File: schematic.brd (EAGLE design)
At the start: 100 x 70 mm, 66 parts, among them U1 ADP3338AKCZ-3.3RL7

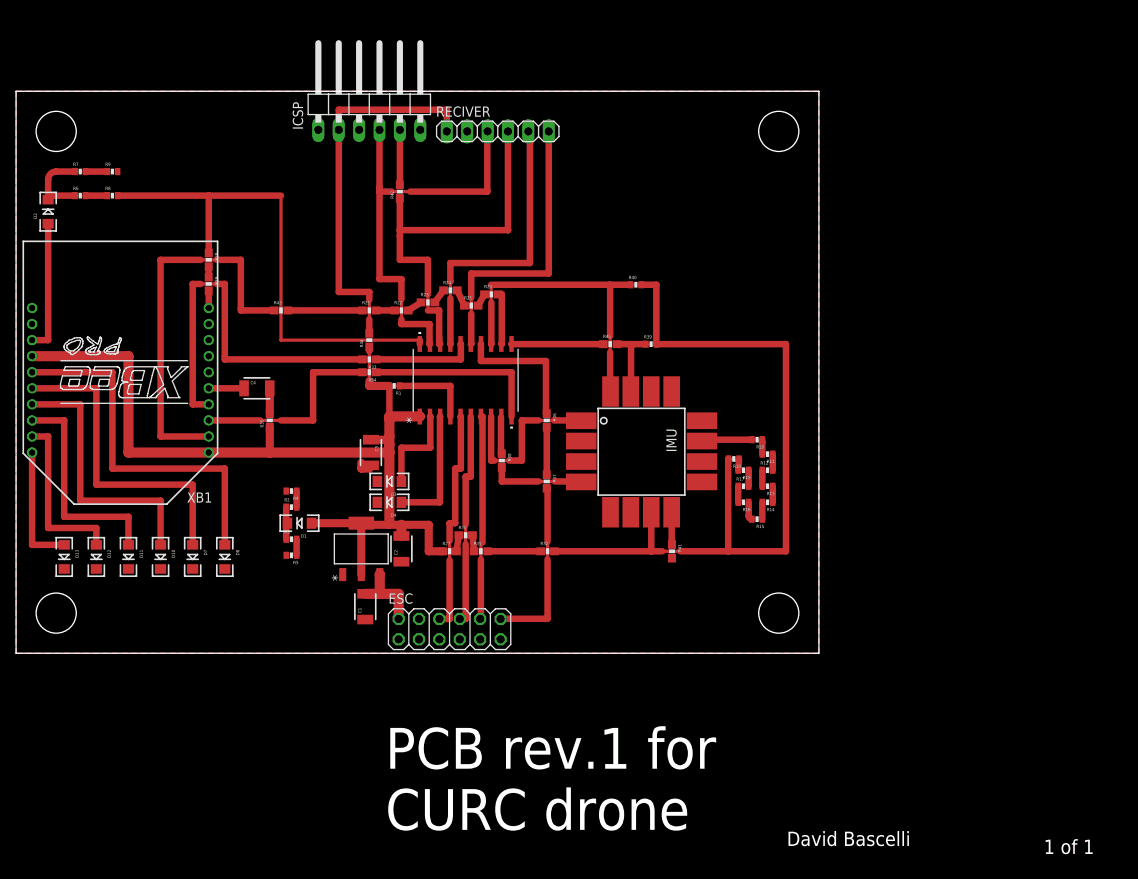
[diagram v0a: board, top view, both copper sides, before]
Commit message: Removed jumper's from schematic and prepared for two layer board
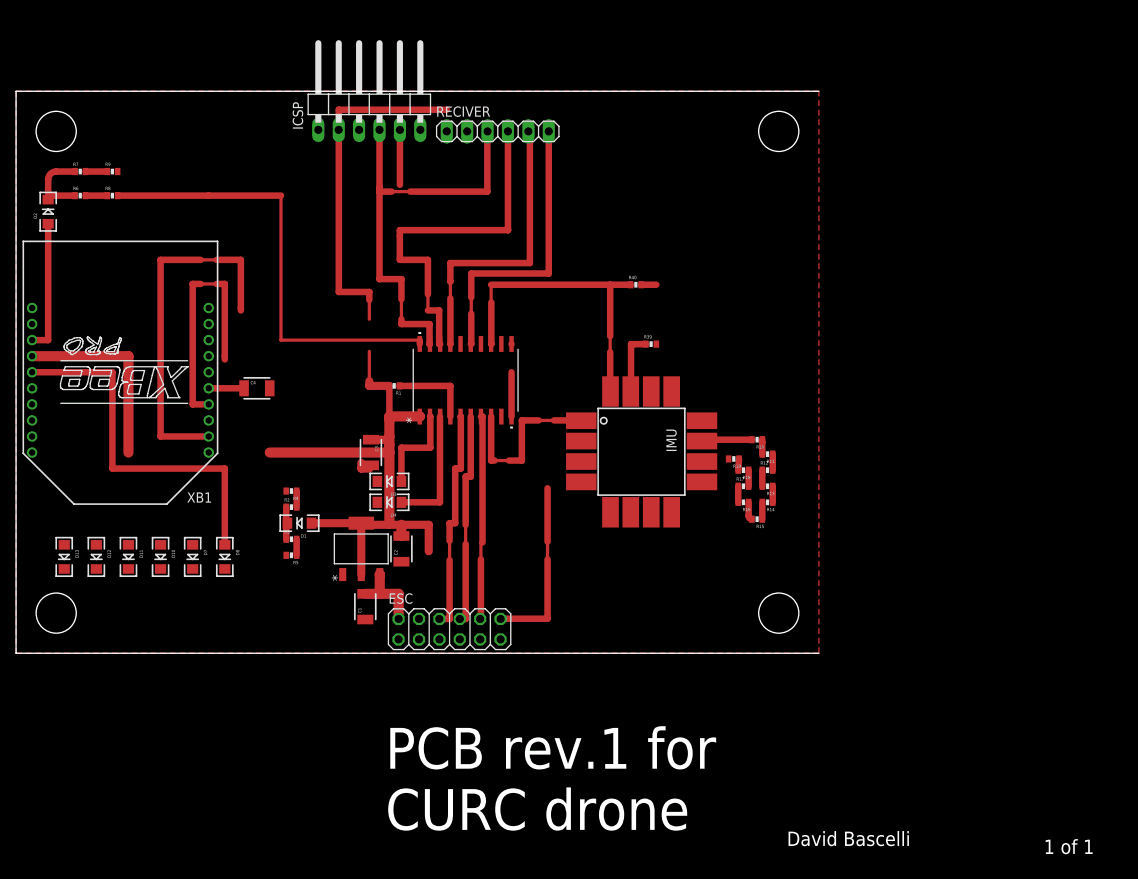
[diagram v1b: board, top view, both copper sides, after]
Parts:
- removed R20, R21, R22, R23, R24, R25, R27, R28, R29, R30, R31, R32, R33, R34, R35, R36, R37, R38, R41, R42, R43, R44, R45: 0, SparkFun-Passives:0603-RES
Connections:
- removed net GND_S: R29.2, XB1.10
- removed net N$1 (its old number): R20.1, R25.2
- removed net N$20 (its old number): R21.2, R22.1
- removed net N$21 (its old number): R22.2, R23.1
- removed net N$22 (its old number): R23.2, R24.1
- removed net N$23 (its old number): R24.2, R25.1
- removed net N$24: R28.2, R29.1
- removed net N$25: MAIN_CONTROLLER.16, R33.1
- removed net N$27: R27.2, R30.1
- removed net N$28: R30.2, R31.1
- removed net N$29: R31.2, R32.1
- removed net N$30: R34.2, XB1.3
- removed net N$31: C4.2, R35.2
- removed net N$32: MAIN_CONTROLLER.14, R36.1
- removed net N$33: R36.2, R37.1
- removed net N$34: IMU.P$4, R38.2
- removed net N$35: IMU.P$8, R41.1
- removed net N$36: R21.1, R43.2
- removed net N$37: ICSP.5, R42.2
- removed net N$38: ICSP.2, R44.2, RECIVER.1
- removed net N$39: MAIN_CONTROLLER.11, R45.1
- removed net N$45: XB1.11
- removed net RX_S: MAIN_CONTROLLER.12, R20.2
- removed net VDD_S: IMU.P$7, R19.2, R32.2, R39.2, R40.2
- net GND: now also IMU.P$8, XB1.10; no longer R28.1, R41.2
- net IMU_INT: now also IMU.P$4; no longer R38.1
- net M4: now also MAIN_CONTROLLER.14; no longer R37.2
- net PGC/ROLL: now also ICSP.5; no longer R42.1
- net RX: now also MAIN_CONTROLLER.12; no longer R43.1
- net SCL: now also MAIN_CONTROLLER.11; no longer R45.2
- net TX: now also XB1.3; no longer R34.1
- net VDD: now also C4.2, ICSP.2, IMU.P$7, R19.2, R39.2, R40.2, RECIVER.1; no longer R27.1, R35.1, R44.1
- net XBEE_INT: now also MAIN_CONTROLLER.16; no longer R33.2
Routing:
- net VDD_S: track 96.5 -> 0.00 mm
- net N$38: track 47.8 -> 0.00 mm
- net N$1: track 39.5 -> 0.00 mm
- net N$20: track 33.5 -> 0.00 mm
- net N$21: track 27.5 -> 0.00 mm
- net N$30: track 25.1 -> 0.00 mm
- net VDD: track 118.8 -> 141.0 mm
- net N$22: track 21.5 -> 0.00 mm
- net XBEE_INT: track 47.5 -> 30.4 mm
- net N$32: track 16.9 -> 0.00 mm
- net TX: track 22.4 -> 5.52 mm
- net N$23: track 15.5 -> 0.00 mm
- net N$25: track 12.5 -> 0.00 mm
- net N$34: track 11.7 -> 0.00 mm
- net N$39: track 11.5 -> 0.00 mm
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
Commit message: Made the two layer board.
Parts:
- added UART: (no value), SparkFun-Connectors:1X03_LONGPADS
- moved R40 23.4 mm to (65.7, 25.5), turned to 180 degrees
- moved R39 16.9 mm to (65.7, 28.2), turned to 180 degrees
- moved R10 13.9 mm to (87.3, 13.6)
- moved IMU 13.9 mm to (64.0, 21.0)
- moved R11 13.9 mm to (88.6, 11.8)
- moved R12 13.9 mm to (88.6, 9.80)
- moved R13 13.9 mm to (88.6, 7.80)
- moved R14 13.9 mm to (88.6, 5.80)
- moved R15 13.9 mm to (87.3, 3.70)
- moved R16 13.9 mm to (85.6, 5.80)
- moved R17 13.9 mm to (85.6, 7.80)
- moved R18 13.9 mm to (85.6, 9.80)
- moved R19 13.9 mm to (84.4, 11.2)
- moved D4 7.31 mm to (52.8, 22.5), turned to 270 degrees
- moved C3 3.16 mm to (43.2, 22.0), turned to 180 degrees
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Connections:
- net GND: now also UART.3
- net RX: now also UART.1
- net TX: now also UART.2
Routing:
- net VDD: track 141.0 -> 258.5 mm, vias 0 -> 6
- net TX: track 5.52 -> 48.7 mm, vias 0 -> 1
- net N$1: track 0.00 -> 40.5 mm
- net N$20: track 0.00 -> 34.5 mm
- net GND: track 58.1 -> 92.1 mm, vias 0 -> 6
- net M4: track 22.1 -> 54.3 mm, vias 0 -> 1
- net N$21: track 0.00 -> 28.5 mm
- net SCL: track 7.80 -> 34.0 mm
- net IMU_INT: track 0.00 -> 26.1 mm, vias 0 -> 2
- net N$22: track 0.00 -> 22.5 mm
- net N$23: track 0.00 -> 16.7 mm
- net XBEE_INT: track 30.4 -> 43.3 mm, vias 0 -> 1
- net PGC/ROLL: track 51.8 -> 63.5 mm, vias 0 -> 1
- net N$41: track 15.5 -> 5.50 mm
- net RX: track 44.3 -> 51.0 mm, vias 0 -> 2
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- added copper zone on layer 16, net GND

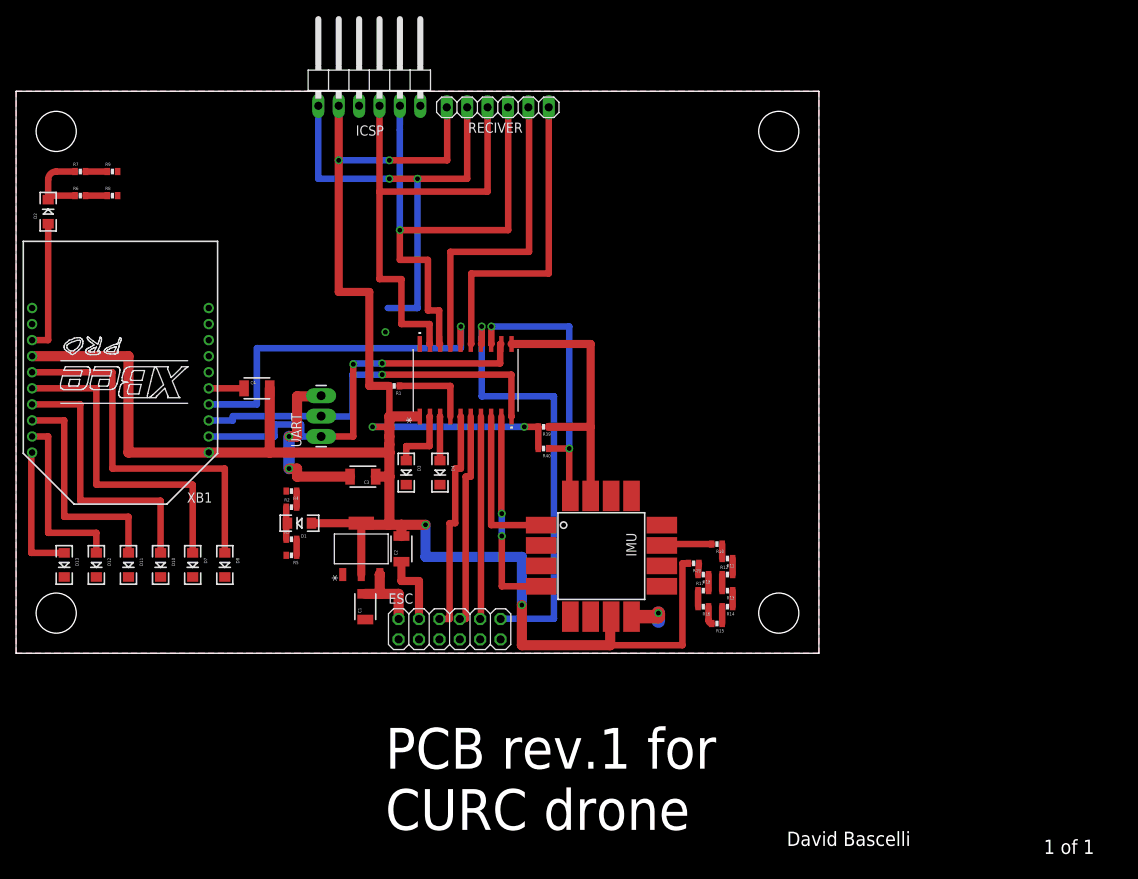
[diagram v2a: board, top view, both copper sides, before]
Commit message: Added curc logo to silkscreen
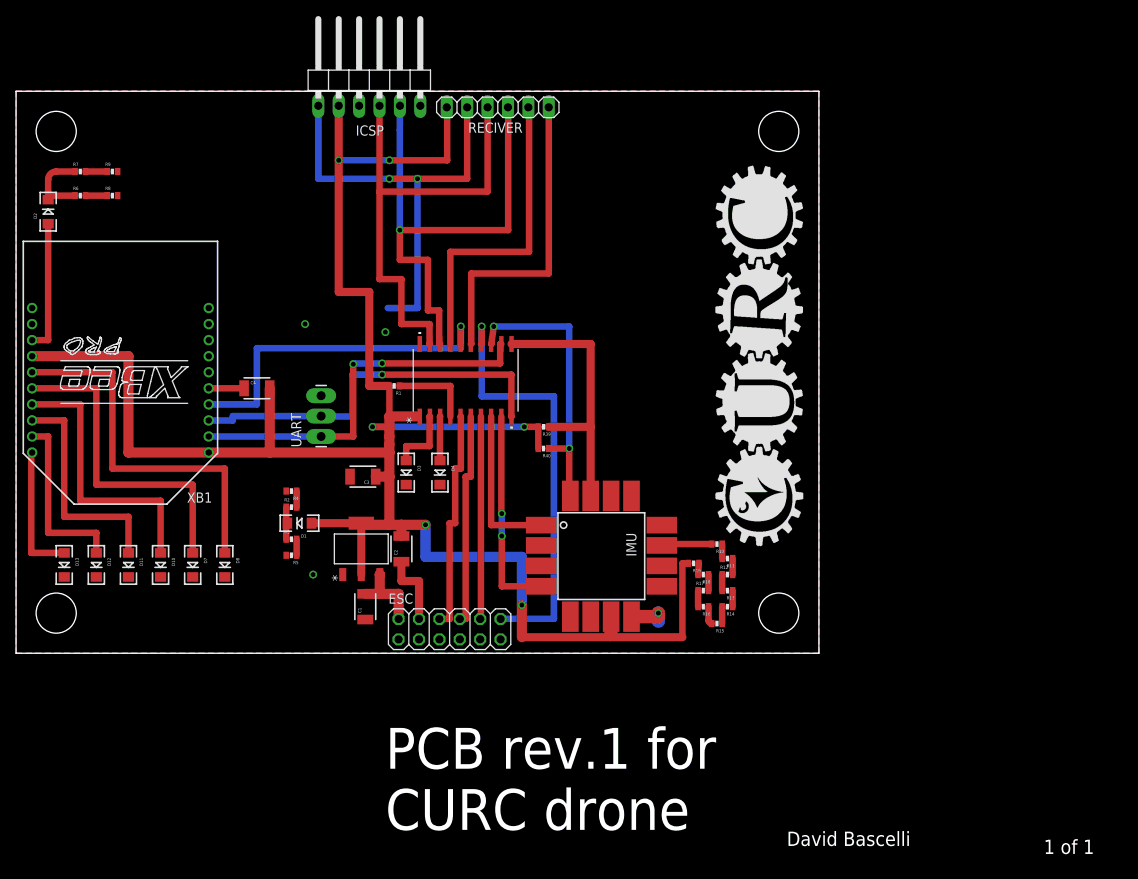
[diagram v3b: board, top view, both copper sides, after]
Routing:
- net GND: track 92.1 -> 70.4 mm
- net VDD: track 258.5 -> 255.7 mm
- net RX: track 51.0 -> 48.4 mm

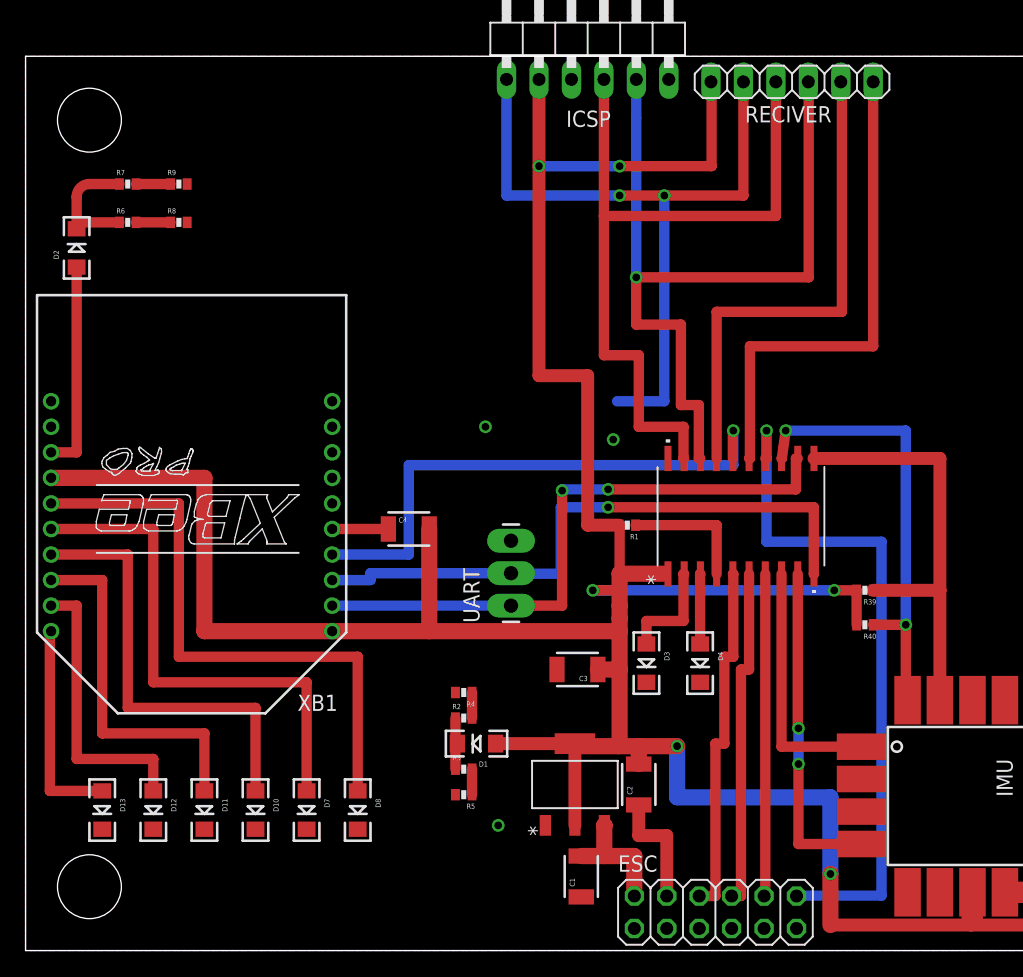
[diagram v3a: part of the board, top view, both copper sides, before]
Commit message: Mitered all wires.
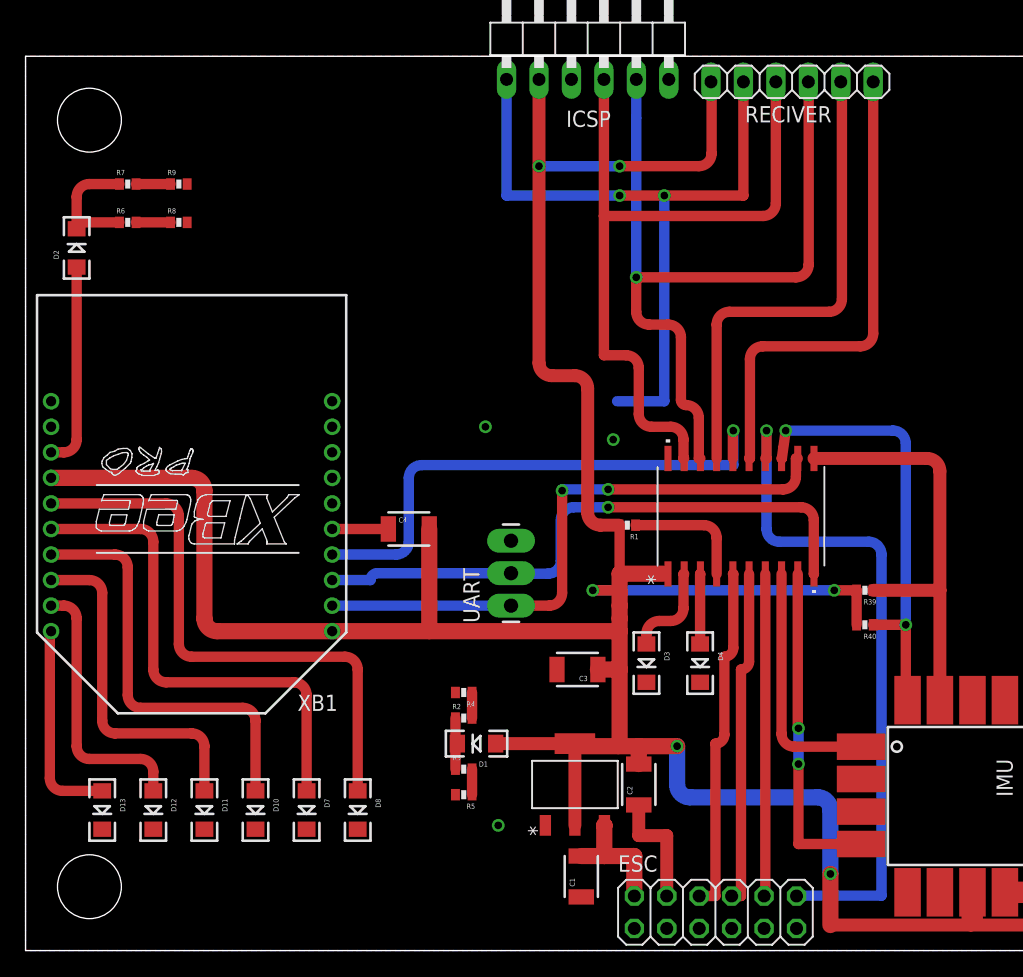
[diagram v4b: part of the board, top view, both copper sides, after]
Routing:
- net VDD: track 255.7 -> 251.1 mm
- net PGC/ROLL: track 63.5 -> 60.9 mm
- net PGD/PITCH: track 59.9 -> 57.6 mm
- net TX: track 48.7 -> 46.6 mm
- net N$44: track 46.5 -> 44.7 mm
- net N$22: track 22.5 -> 20.7 mm
- net N$21: track 28.5 -> 26.7 mm
- net N$20: track 34.5 -> 32.7 mm
- net N$1: track 40.5 -> 38.7 mm
- net M4: track 54.3 -> 53.2 mm
- net N$40: track 8.43 -> 7.26 mm
- net YAW: track 39.4 -> 38.2 mm
- net XBEE_INT: track 43.3 -> 42.1 mm
- net THROTTLE: track 39.2 -> 38.0 mm
- net RX: track 48.4 -> 47.3 mm
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
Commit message: Straightened out some wires
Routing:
- net PGC/ROLL: track 60.9 -> 61.8 mm
- net PGD/PITCH: track 57.6 -> 57.0 mm
- net IMU_INT: track 26.1 -> 25.5 mm
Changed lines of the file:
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@@
 <contactref element="MAIN_CONTROLLER" pad="19"/>
 <wire x1="51.555" y1="38.5212" x2="51.5" y2="38.5212" width="0.8128" layer="1"/>
-<wire x1="45.27" y1="46.6" x2="45.27" y2="57.5" width="0.8128" layer="1"/>
+<wire x1="47" y1="46.6" x2="46.27" y2="46.6" width="0.8128" layer="1"/>
+<wire x1="46.27" y1="46.6" x2="45.27" y2="47.6" width="0.8128" layer="1" curve="-90"/>
+<wire x1="45.27" y1="47.6" x2="45.27" y2="57.5" width="0.8128" layer="1"/>
 <wire x1="45.27" y1="57.5" x2="45.27" y2="68.19" width="0.8128" layer="1"/>
 <wire x1="48" y1="45.6" x2="48" y2="42" width="0.8128" layer="1"/>
@@
 <wire x1="51.5" y1="40" x2="51.5" y2="38.5212" width="0.8128" layer="1"/>
 <wire x1="48" y1="45.6" x2="47" y2="46.6" width="0.8128" layer="1" curve="90"/>
-<wire x1="47" y1="46.6" x2="45.27" y2="46.6" width="0.8128" layer="1"/>
 <wire x1="45.27" y1="57.5" x2="57.73" y2="57.5" width="0.8128" layer="1"/>
 <wire x1="57.73" y1="57.5" x2="58.73" y2="58.5" width="0.8128" layer="1" curve="90"/>
@@
 <contactref element="RECIVER" pad="4"/>
 <contactref element="MAIN_CONTROLLER" pad="18"/>
-<wire x1="50.3" y1="49" x2="48.8" y2="49" width="0.8128" layer="1"/>
+<wire x1="51.7" y1="49" x2="48.8" y2="49" width="0.8128" layer="1"/>
 <wire x1="48.8" y1="49" x2="47.8" y2="50" width="0.8128" layer="1" curve="-90"/>
 <wire x1="47.8" y1="50" x2="47.8" y2="52.7" width="0.8128" layer="1"/>
@@
 <wire x1="60.3" y1="52.7" x2="47.8" y2="52.7" width="0.8128" layer="1"/>
 <wire x1="52.825" y1="38.5212" x2="52.7" y2="38.5212" width="0.8128" layer="1"/>
-<wire x1="52.7" y1="38.5212" x2="52.7" y2="41.7" width="0.8128" layer="1"/>
-<wire x1="52.7" y1="41.7" x2="51.7" y2="42.7" width="0.8128" layer="1" curve="90"/>
-<wire x1="51.7" y1="42.7" x2="51.3" y2="43.1" width="0.8128" layer="1" curve="-90"/>
-<wire x1="51.3" y1="43.1" x2="51.3" y2="48" width="0.8128" layer="1"/>
-<wire x1="51.3" y1="48" x2="50.3" y2="49" width="0.8128" layer="1" curve="90"/>
+<wire x1="52.7" y1="38.5212" x2="52.7" y2="41.6" width="0.8128" layer="1"/>
 <contactref element="ICSP" pad="5"/>
+<wire x1="52.7" y1="41.6" x2="52.7" y2="41.7" width="0.8128" layer="1"/>
 <wire x1="47.81" y1="68.19" x2="47.8" y2="65.19" width="0.8128" layer="16"/>
 <wire x1="61.27" y1="68" x2="61.3" y2="68" width="0.8128" layer="1"/>
 <via x="47.8" y="52.7" extent="1-16" drill="0.6"/>
 <wire x1="47.8" y1="52.7" x2="47.8" y2="65.19" width="0.8128" layer="16"/>
+<wire x1="51.7" y1="49" x2="52.7" y2="48" width="0.8128" layer="1" curve="-90"/>
+<wire x1="52.7" y1="48" x2="52.7" y2="41.7" width="0.8128" layer="1"/>
 </signal>
 <signal name="SCL">
@@
 <contactref element="MAIN_CONTROLLER" pad="9"/>
 <contactref element="IMU" pad="P$4"/>
-<wire x1="65.4" y1="8.34" x2="60.5" y2="8.34" width="0.8128" layer="1"/>
-<wire x1="60.5" y1="8.34" x2="60.5" y2="14.6" width="0.8128" layer="1"/>
+<wire x1="65.4" y1="8.34" x2="61.5" y2="8.34" width="0.8128" layer="1"/>
+<wire x1="61.5" y1="8.34" x2="60.5" y2="9.34" width="0.8128" layer="1" curve="-90"/>
+<wire x1="60.5" y1="9.34" x2="60.5" y2="14.6" width="0.8128" layer="1"/>
 <via x="60.5" y="14.6" extent="1-16" drill="0.6"/>
 <wire x1="60.5" y1="14.6" x2="60.5" y2="17.4" width="0.8128" layer="16"/>
